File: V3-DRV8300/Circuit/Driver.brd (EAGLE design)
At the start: 63.5 x 55.5 mm, 37 parts, among them IC1 DRV8303DCA

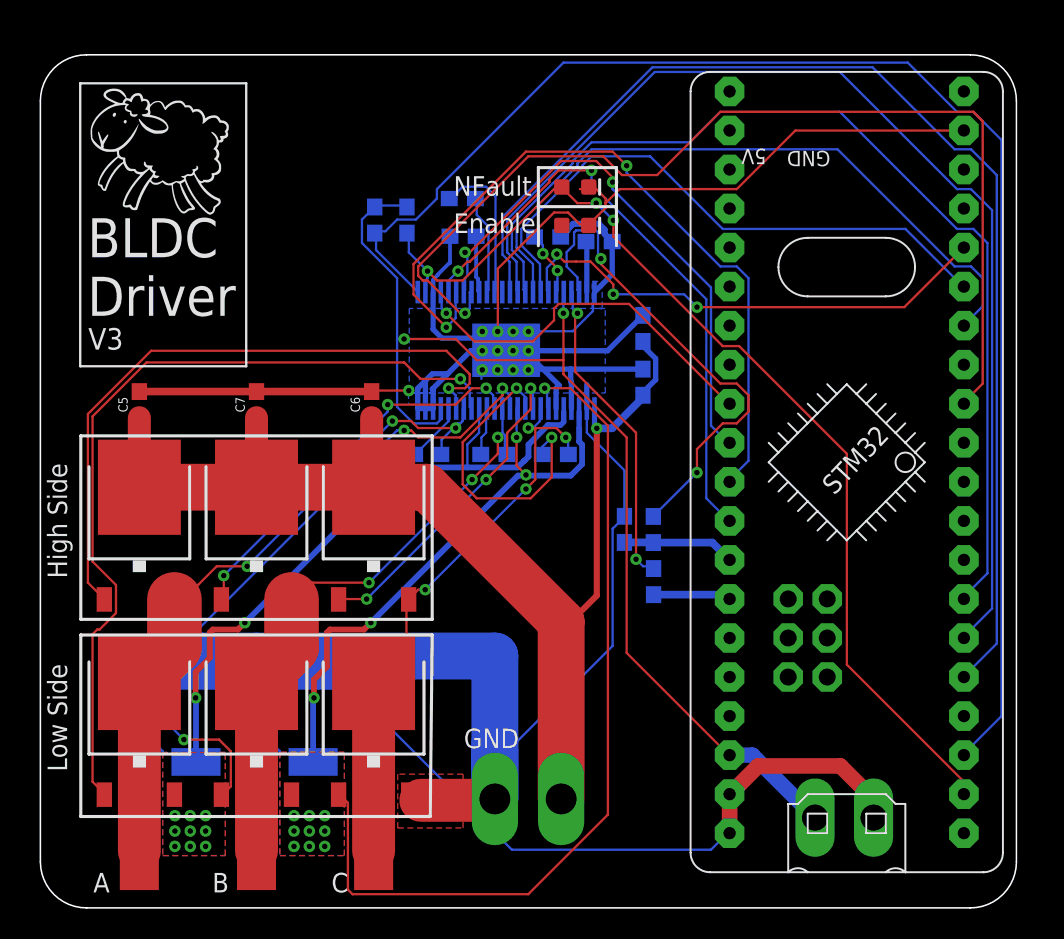
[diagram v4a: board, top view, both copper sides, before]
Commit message: Moving two vias, the AGND signal have a better conductivity to the power pad
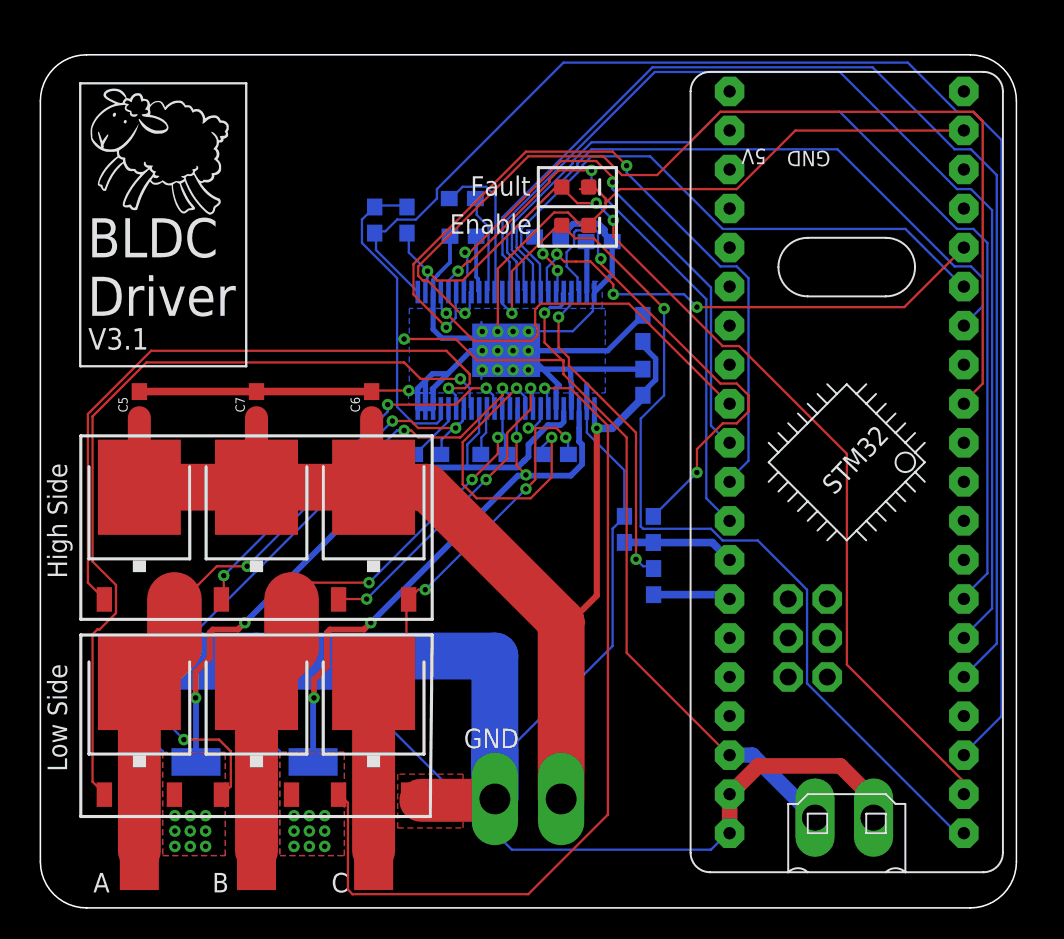
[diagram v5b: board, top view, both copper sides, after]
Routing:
- net PB12: track 0.00 -> 65.4 mm, vias 0 -> 2
- net VCC: track 74.1 -> 75.5 mm
- net PA4: track 24.9 -> 25.7 mm
- net N$1: track 20.7 -> 21.4 mm
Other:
- board text added: "Fault"
- board text added: "V3.1"
- board text removed: "NFault"
- board text removed: "V3"

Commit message: Generated the V3.1 DRV8303 Gerber files
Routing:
- net GND: track 260.1 -> 273.9 mm
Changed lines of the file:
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@@
 <wire x1="35.2044" y1="42.9768" x2="35.177" y2="42.9" width="0.1524" layer="1"/>
 <wire x1="35.3568" y1="45.5676" x2="35.177" y2="45.4" width="0.1524" layer="1"/>
-<wire x1="28.194" y1="32.9184" x2="28.194" y2="33.3756" width="0.1524" layer="16"/>
 <wire x1="28.194" y1="33.3756" x2="28.25" y2="33.5" width="0.1524" layer="16"/>
 <wire x1="31.3944" y1="33.528" x2="29.8" y2="34.777" width="0.1524" layer="16"/>
 <wire x1="31.3944" y1="33.528" x2="31.25" y2="33.5" width="0.1524" layer="16"/>
-<wire x1="29.718" y1="33.528" x2="29.2608" y2="33.528" width="0.1524" layer="16"/>
 <wire x1="29.2608" y1="33.528" x2="29.25" y2="33.5" width="0.1524" layer="16"/>
-<wire x1="29.718" y1="33.528" x2="29.8" y2="34.777" width="0.1524" layer="16"/>
 <wire x1="29.2608" y1="36.616996875" x2="29.2608" y2="36.1188" width="0.1524" layer="16"/>
 <wire x1="29.2608" y1="36.1188" x2="29.25" y2="36" width="0.1524" layer="16"/>
@@
 <wire x1="21.336" y1="32.1564" x2="21.053" y2="32.092" width="0.1524" layer="1"/>
 <wire x1="23.4696" y1="32.1564" x2="23.5" y2="32.1564" width="0.1524" layer="16"/>
-<wire x1="36.7284" y1="15.5448" x2="30.48" y2="9.2964" width="0.1524" layer="16"/>
-<wire x1="36.7284" y1="23.1648" x2="36.7284" y2="15.5448" width="0.1524" layer="16"/>
-<wire x1="37.4904" y1="23.9268" x2="36.7284" y2="23.1648" width="0.1524" layer="16"/>
 <wire x1="30.48" y1="9.2964" x2="29.07" y2="9.2964" width="0.1524" layer="16"/>
 <wire x1="37.4904" y1="23.9268" x2="37.5" y2="23.977" width="0.1524" layer="16"/>
@@
 <wire x1="29.2608" y1="36.1188" x2="29.25" y2="36" width="0.1524" layer="1"/>
 <polygon width="0.1" layer="16">
-<vertex x="35.4" y="37.5"/>
+<vertex x="35.4" y="37.2"/>
 <vertex x="35.4" y="39.25"/>
-<vertex x="36.1" y="39.25"/>
-<vertex x="36.05" y="39.2"/>
-<vertex x="36.05" y="37.45"/>
-<vertex x="36" y="37.5"/>
+<vertex x="36.3" y="39.25"/>
+<vertex x="36.3" y="37.2"/>
 </polygon>
 <polygon width="0.1" layer="16">
@@
 <wire x1="28.194" y1="36.616996875" x2="28.194" y2="36.1188" width="0.1524" layer="16"/>
 <wire x1="28.194" y1="36.1188" x2="28.25" y2="36" width="0.1524" layer="16"/>
+<wire x1="35.05" y1="30.989" x2="35.0576" y2="30.9814" width="0.3" layer="16"/>
+<wire x1="37.4904" y1="26.94708125" x2="37.4904" y2="23.9268" width="0.3" layer="16"/>
+<wire x1="35.0576" y1="30.9814" x2="35.0576" y2="29.37988125" width="0.3" layer="16"/>
+<wire x1="35.0576" y1="29.37988125" x2="37.4904" y2="26.94708125" width="0.3" layer="16"/>
+<wire x1="37.5" y1="23.977" x2="37.5" y2="23.75465625" width="0.3" layer="16"/>
+<wire x1="37.5" y1="23.75465625" x2="36.6976" y2="22.95225625" width="0.3" layer="16"/>
+<wire x1="36.6976" y1="13.2156" x2="29.07" y2="5.588" width="0.3" layer="16"/>
+<wire x1="36.6976" y1="22.95225625" x2="36.6976" y2="13.2156" width="0.3" layer="16"/>
+<wire x1="29.8" y1="34.777" x2="29.2608" y2="34.2378" width="0.3" layer="16"/>
+<wire x1="29.2608" y1="34.2378" x2="29.2608" y2="33.528" width="0.3" layer="16"/>
+<wire x1="29.8" y1="34.777" x2="28.523" y2="33.5" width="0.3" layer="16"/>
+<wire x1="28.523" y1="33.5" x2="28.25" y2="33.5" width="0.3" layer="16"/>
 </signal>
 <signal name="N$4">
@@
 <contactref element="C14" pad="1"/>
 <contactref element="C15" pad="1"/>
-<via x="35.7" y="29.7" extent="1-16" drill="0.35"/>
+<via x="35.8" y="29.6" extent="1-16" drill="0.35"/>
 <wire x1="35.55" y1="30.989" x2="35.55" y2="29.85" width="0.34" layer="16"/>
-<wire x1="35.55" y1="29.85" x2="35.7" y2="29.7" width="0.38" layer="16"/>
+<wire x1="35.55" y1="29.85" x2="35.8" y2="29.6" width="0.38" layer="16"/>
 <wire x1="33.3756" y1="16.3068" x2="33.3" y2="16.3068" width="0.1524" layer="1"/>
 <wire x1="33.3756" y1="16.3068" x2="33.3766375" y2="16.498503125" width="0.1524" layer="1"/>
 <wire x1="33.3766375" y1="16.498503125" x2="33.38" y2="17.12" width="0.1524" layer="1"/>
 <wire x1="38.7" y1="31.85" x2="38.7" y2="31.7" width="0.5" layer="16"/>
-<wire x1="38.7" y1="31.7" x2="36.7" y2="29.7" width="0.5" layer="16"/>
-<wire x1="36.7" y1="29.7" x2="35.7" y2="29.7" width="0.5" layer="16"/>
+<wire x1="38.7" y1="31.7" x2="36.6" y2="29.6" width="0.5" layer="16"/>
+<wire x1="36.6" y1="29.6" x2="35.8" y2="29.6" width="0.5" layer="16"/>
 <wire x1="39.5274" y1="34.2356125" x2="39.5274" y2="32.8643875" width="0.35" layer="16"/>
 <wire x1="38.7" y1="35.35" x2="38.7" y2="35.0630125" width="0.35" layer="16"/>
@@
 <wire x1="38.7" y1="35.0630125" x2="39.5274" y2="34.2356125" width="0.35" layer="16"/>
 <wire x1="39.5274" y1="32.8643875" x2="38.7" y2="32.0369875" width="0.35" layer="16"/>
-<wire x1="35.7" y1="29.7" x2="35.7" y2="18.821865625" width="0.4" layer="1"/>
-<wire x1="35.7" y1="18.821865625" x2="33.3766375" y2="16.498503125" width="0.4" layer="1"/>
+<wire x1="35.8" y1="29.6" x2="35.8" y2="18.921865625" width="0.4" layer="1"/>
+<wire x1="35.8" y1="18.921865625" x2="33.3766375" y2="16.498503125" width="0.4" layer="1"/>
 </signal>
 <signal name="PB12">
